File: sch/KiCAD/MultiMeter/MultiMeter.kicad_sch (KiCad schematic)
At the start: 21 parts, among them J1 Conn_01x02_Male, J10 Conn_01x04_Female, J2 Conn_01x02_Male, J3 Conn_01x03_Male, J4 Conn_01x03_Male, J5 Conn_01x03_Female, J6 Conn_01x15, J7 Conn_01x15, J8 Conn_01x08_Female, J9 Conn_01x02_Female, Q1 2SC1815, Q2 2SC1815

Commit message: 回路図修正中
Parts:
- added A2: Arduino_Nano_v3.x, Module:Arduino_Nano, symbol MCU_Module:Arduino_Nano_v3.x
- added J11: Conn_01x08_Female, Connector_JST:JST_XH_S8B-XH-A-1_1x08_P2.50mm_Horizontal, symbol Connector:Conn_01x08_Female
- added J12: Conn_01x04_Female, Connector_Molex:Molex_SPOX_5268-04A_1x04_P2.50mm_Horizontal, symbol Connector:Conn_01x04_Female
- added J13: Conn_01x15, Connector_PinSocket_2.54mm:PinSocket_1x15_P2.54mm_Vertical, symbol Connector_Generic:Conn_01x15
- added J14: Conn_01x03_Pin, Connector_PinHeader_2.54mm:PinHeader_1x03_P2.54mm_Vertical, symbol Connector:Conn_01x03_Pin
- added SW1, SW2, SW3: SW_Push, Button_Switch_THT:SW_PUSH_6mm, symbol Switch:SW_Push
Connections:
- net GNDPWR is gone; now on net +5V: A1.29 (GND), A1.4 (GND), D5.1 (K), J10.4 (Pin_4), J3.3 (Pin_3), J4.3 (Pin_3), J6.4 (Pin_4), J7.14 (Pin_14), J8.2 (Pin_2), J9.2 (Pin_2), R1.2, R2.2, RV1.2
- net +5V: now also A2.27 (+5V), A2.29 (GND), A2.4 (GND), J11.1 (Pin_1), J11.2 (Pin_2), J12.1 (Pin_1), J12.4 (Pin_4), J13.4 (Pin_4), SW1.1, SW2.1, SW3.1
- new net: A2.1 (D1/TX), J12.3 (Pin_3), J13.1 (Pin_1)
- new net: A2.10 (D7), J13.10 (Pin_10)
- new net: A2.11 (D8), J13.11 (Pin_11)
- new net: A2.12 (D9), J13.12 (Pin_12)
- new net: A2.13 (D10), J13.13 (Pin_13)
- new net: A2.14 (D11), J13.14 (Pin_14)
- new net: A2.15 (D12), J13.15 (Pin_15)
- new net: A2.2 (D0/RX), J12.2 (Pin_2), J13.2 (Pin_2)
- new net: A2.23 (A4), J11.4 (Pin_4)
- new net: A2.24 (A5), J11.3 (Pin_3)
- new net: A2.3 (~{RESET}), J13.3 (Pin_3)
- new net: A2.5 (D2), J13.5 (Pin_5)
- new net: A2.6 (D3), J13.6 (Pin_6)
- new net: A2.7 (D4), J13.7 (Pin_7)
- new net: A2.8 (D5), J13.8 (Pin_8)
- new net: A2.9 (D6), J13.9 (Pin_9)
- new net: J14.3 (Pin_3), SW3.2
- new net: J14.1 (Pin_1), SW1.2
- new net: J14.2 (Pin_2), SW2.2
- new net +3.3V: A2.17 (3V3), J11.8 (Pin_8)
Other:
- moved on the sheet: A1, D5, J1, J10, J2, J3, J4, J5, J6, J7, J8, J9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

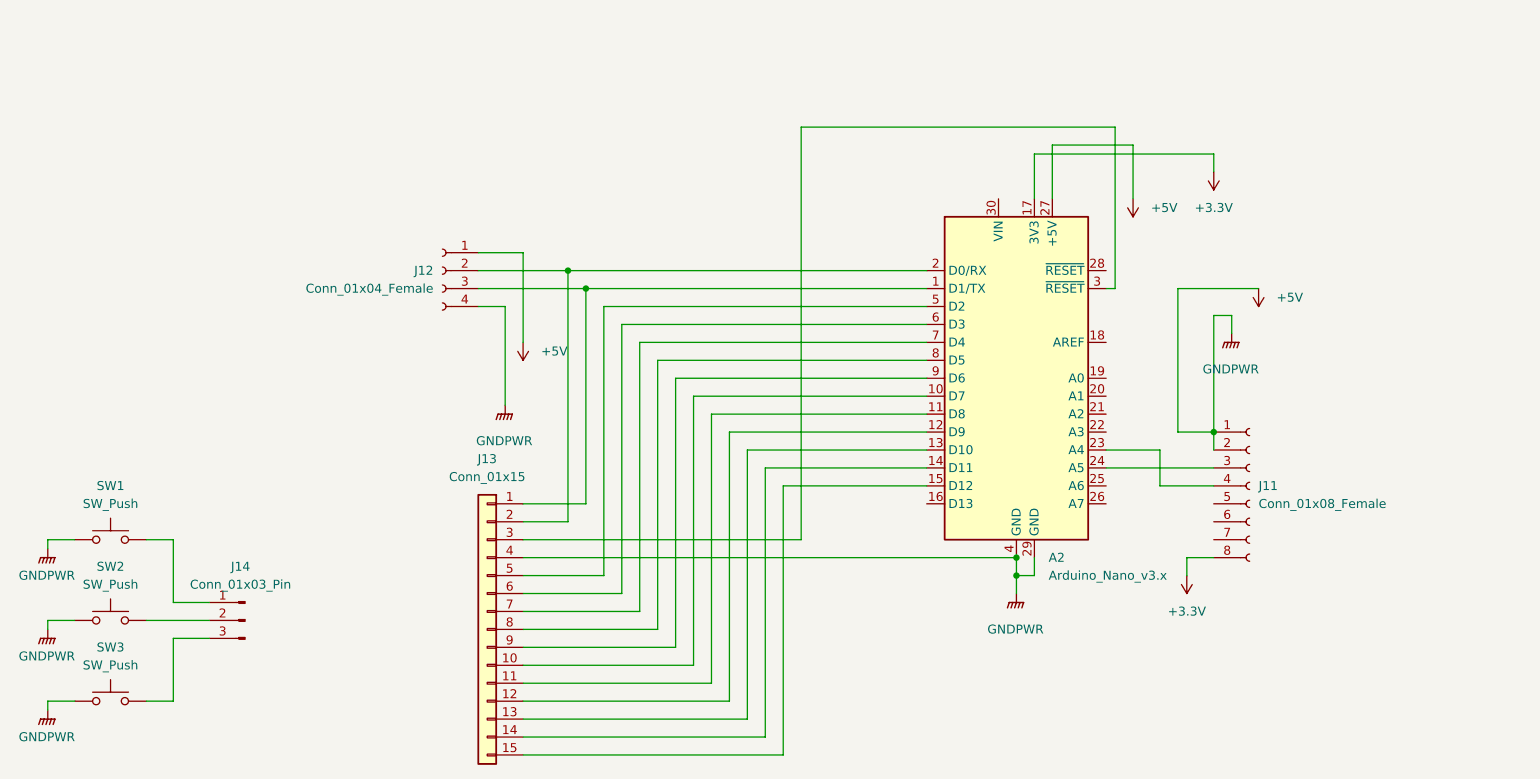
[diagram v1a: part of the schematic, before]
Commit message: 複製した回路図の重複部分を削除
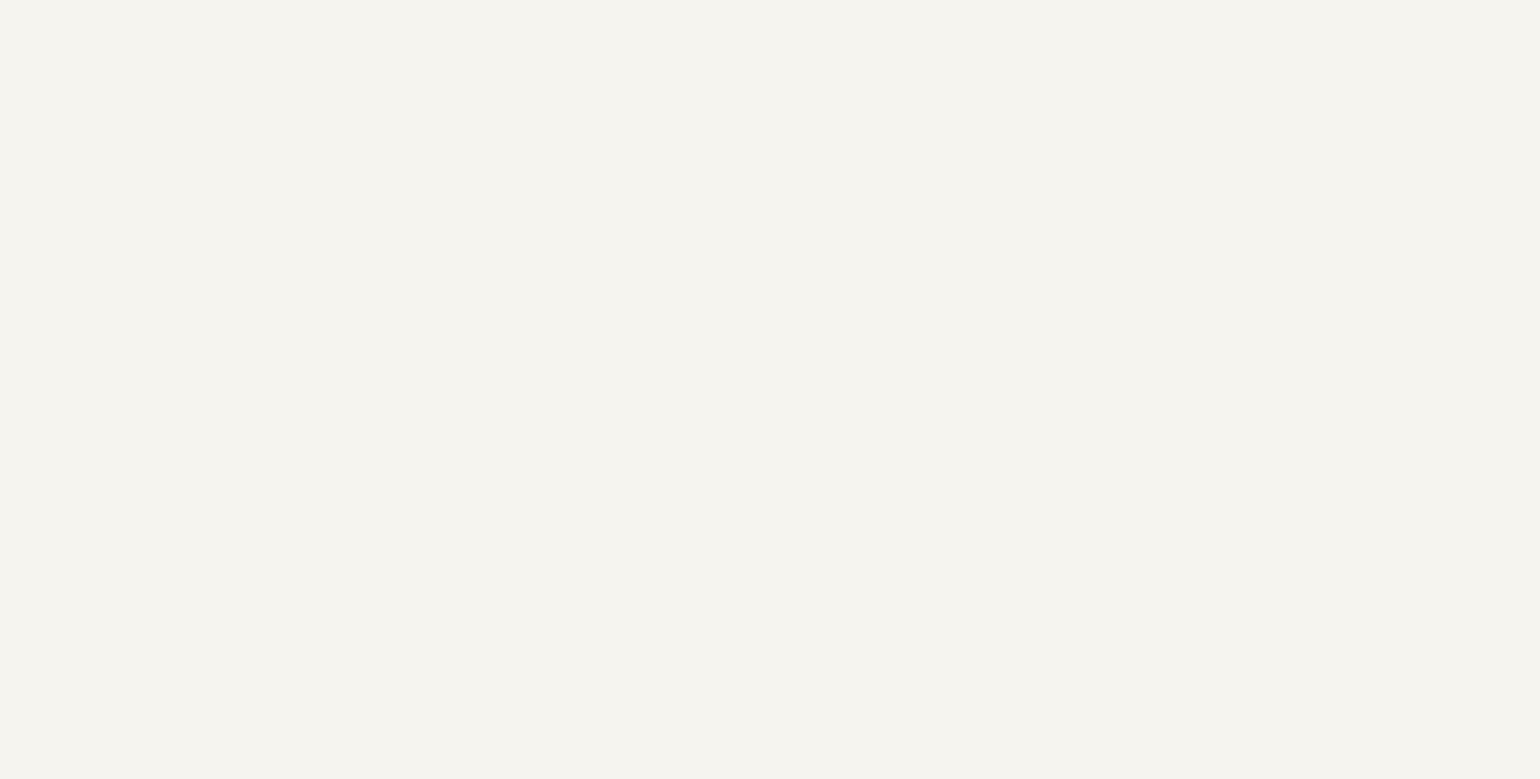
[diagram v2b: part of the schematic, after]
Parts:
- removed A2: Arduino_Nano_v3.x, Module:Arduino_Nano, symbol MCU_Module:Arduino_Nano_v3.x
- removed J11: Conn_01x08_Female, Connector_JST:JST_XH_S8B-XH-A-1_1x08_P2.50mm_Horizontal, symbol Connector:Conn_01x08_Female
- removed J12: Conn_01x04_Female, Connector_Molex:Molex_SPOX_5268-04A_1x04_P2.50mm_Horizontal, symbol Connector:Conn_01x04_Female
- removed J13: Conn_01x15, Connector_PinSocket_2.54mm:PinSocket_1x15_P2.54mm_Vertical, symbol Connector_Generic:Conn_01x15
- removed J14: Conn_01x03_Pin, Connector_PinHeader_2.54mm:PinHeader_1x03_P2.54mm_Vertical, symbol Connector:Conn_01x03_Pin
- removed SW1, SW2, SW3: SW_Push, Button_Switch_THT:SW_PUSH_6mm, symbol Switch:SW_Push
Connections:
- net +5V: no longer A1.29 (GND), A1.4 (GND), D5.1 (K), J10.4 (Pin_4), J3.3 (Pin_3), J4.3 (Pin_3), J6.4 (Pin_4), J7.14 (Pin_14), J8.2 (Pin_2), J9.2 (Pin_2), R1.2, R2.2, RV1.2
- new net GNDPWR: A1.29 (GND), A1.4 (GND), D5.1 (K), J10.4 (Pin_4), J3.3 (Pin_3), J4.3 (Pin_3), J6.4 (Pin_4), J7.14 (Pin_14), J8.2 (Pin_2), J9.2 (Pin_2), R1.2, R2.2, RV1.2
